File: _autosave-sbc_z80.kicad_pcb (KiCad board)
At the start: 4 copper layers, 102.6 x 50.8 mm, 95 parts, among them J1 RC80 Bus, J2 CTC Header, J3 AVR-JTAG-10, J4 IDE, J5 PIO Header, J6 Port A, J7 Port B, J8 USB_B_Micro, Q1 IRLML6402, SW1 Reset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

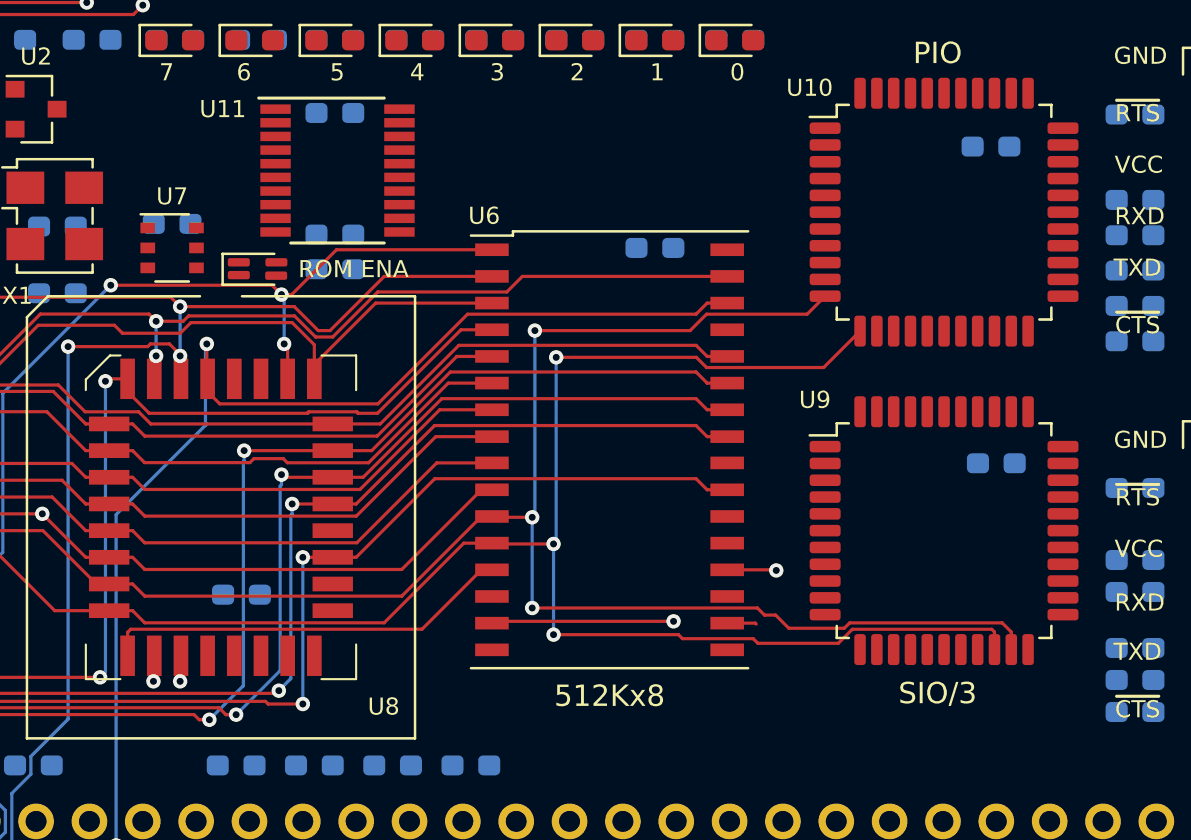
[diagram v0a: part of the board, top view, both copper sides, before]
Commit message: data lines on inner layers
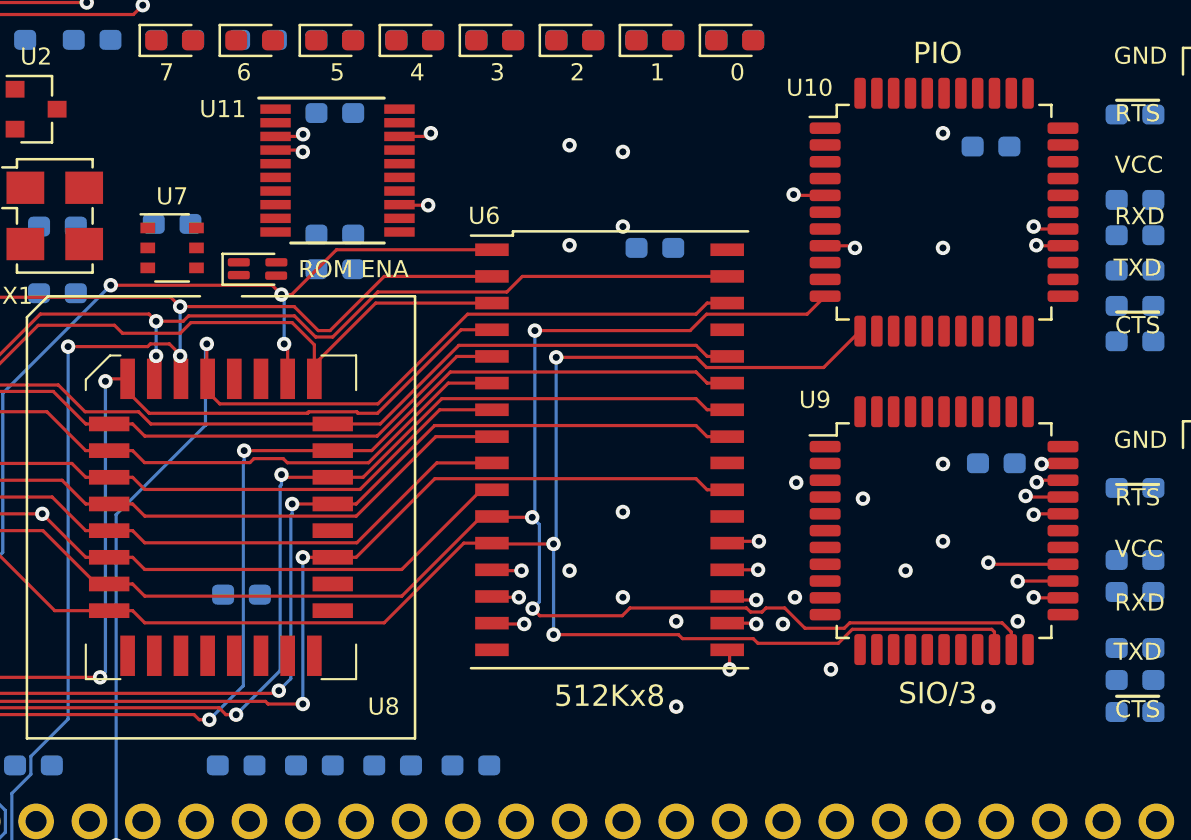
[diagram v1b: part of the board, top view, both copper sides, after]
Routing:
- net /D1: track 1.23 -> 97.3 mm, vias 1 -> 8
- net /D7: track 0.00 -> 80.4 mm, vias 0 -> 8
- net /D4: track 1.40 -> 68.5 mm, vias 0 -> 6
- net /D0: track 19.2 -> 74.0 mm, vias 0 -> 6
- net /D2: track 9.98 -> 43.9 mm, vias 2 -> 5
- net /D5: track 0.00 -> 33.1 mm, vias 0 -> 4
- net /D3: track 0.00 -> 31.4 mm, vias 0 -> 4
- net /D6: track 2.35 -> 28.8 mm, vias 1 -> 3
- net /A1: track 168.9 -> 169.6 mm
